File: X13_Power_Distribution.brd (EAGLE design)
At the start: 152.4 x 73.7 mm, 44 parts, among them Q1 IRF1018EPBF, Q2 SSM3K341R, Q3 IRF1018EPBF, Q4 IRF1018EPBF, Q5 SSM3K341R, Q6 SSM3K341R, U1 LM74610, U2 LM74610, U3 LM5050, U4 LM5050

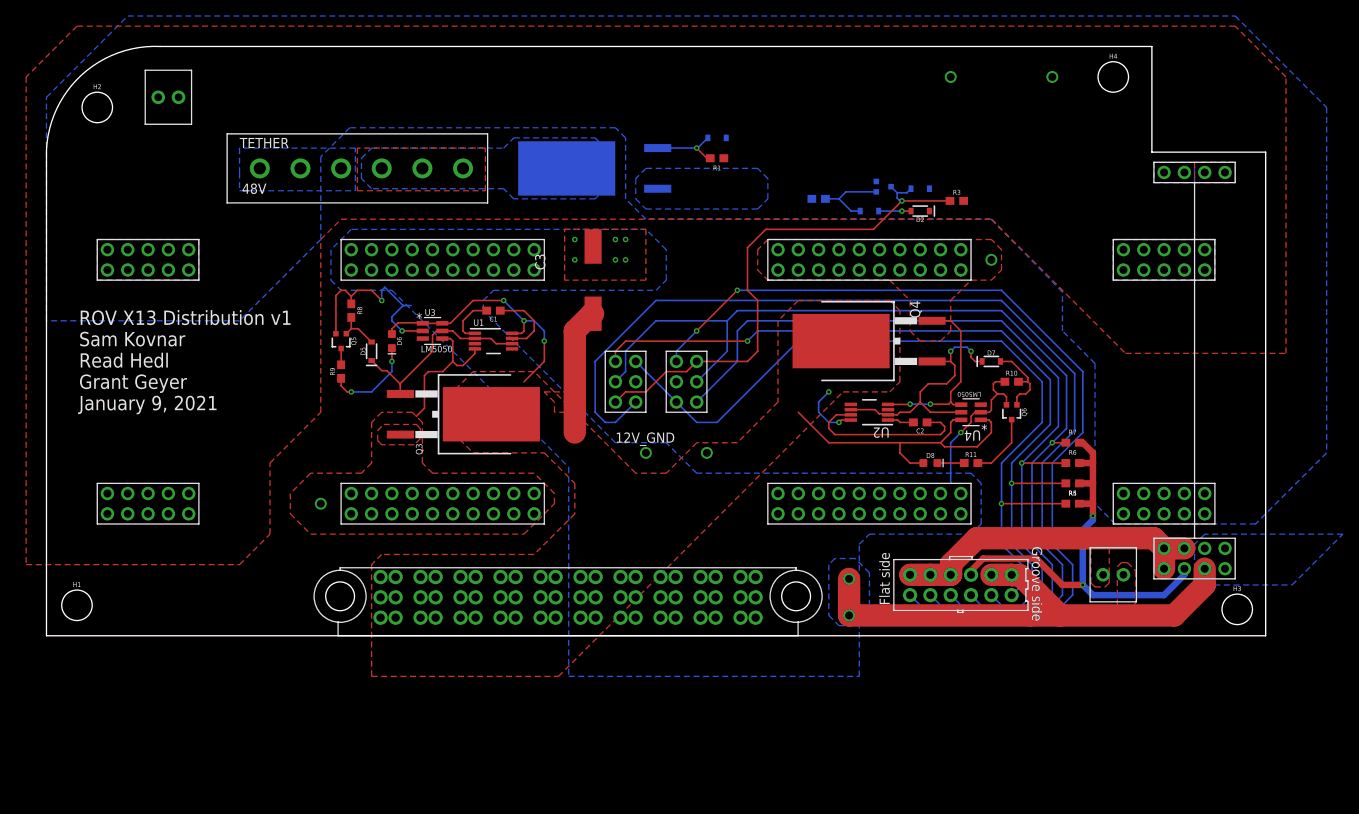
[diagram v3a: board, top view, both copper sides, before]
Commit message: Made some slight changes to thermals
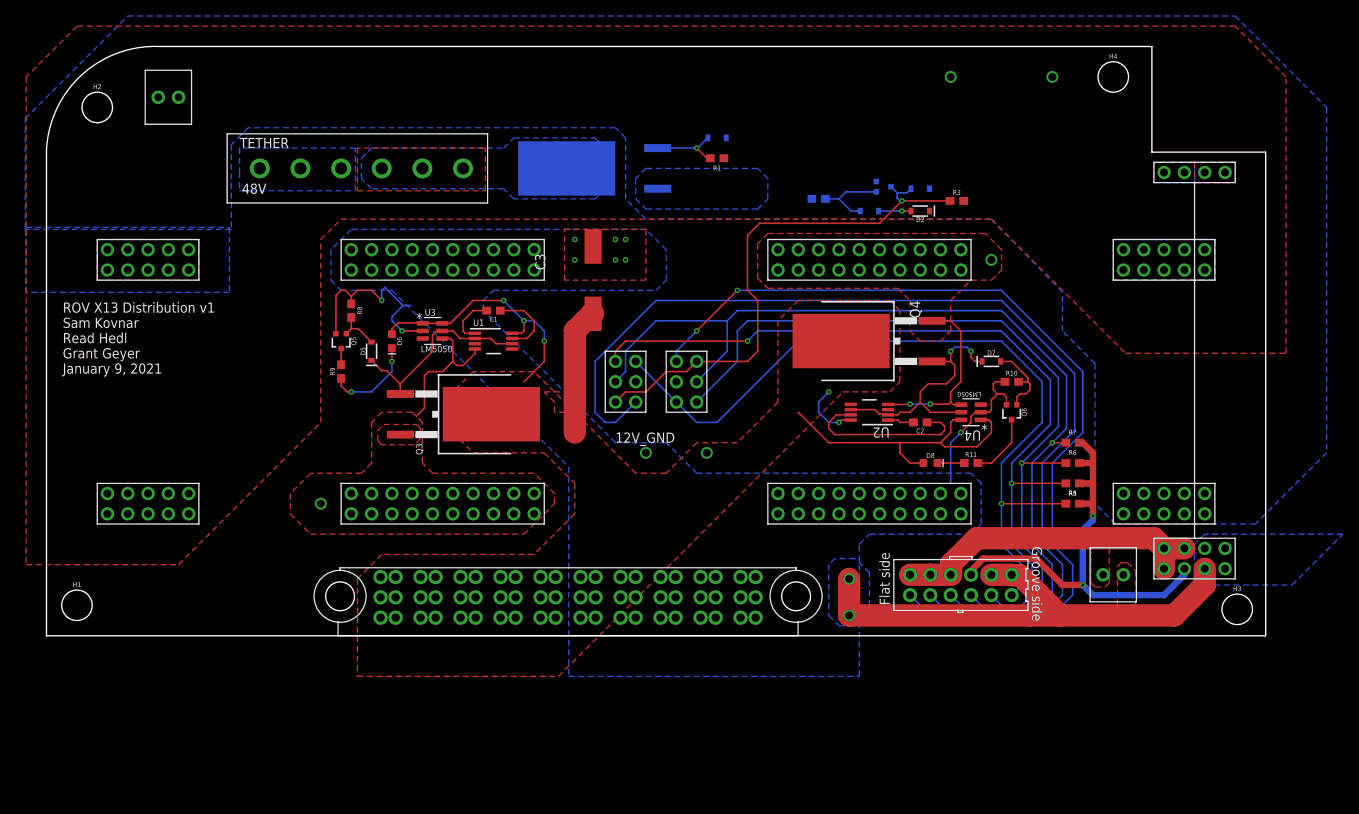
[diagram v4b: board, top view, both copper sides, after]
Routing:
- net ON/OFF: track 66.1 -> 67.0 mm

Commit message: Some more edits
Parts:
- added +12V_A_TEST, +12V_B_TEST, +12V_TEST, +48V_TEST, 12_GND, 48GND_TEST: SSW-101-02-G-S, con-samtec:SSW-101-02-G-S
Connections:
- net +12V: now also +12V_TEST.1
- net +12V_A: now also +12V_A_TEST.1
- net +12V_B: now also +12V_B_TEST.1
- net +48V: now also +48V_TEST.1
- net 12V_GND: now also 12_GND.1
- net 48V_GND: now also 48GND_TEST.1
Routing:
- net +48V: track 0.00 -> 15.6 mm
- net 12V_GND: vias 10 -> 9
- net +12V_B: vias 3 -> 2
- net +12V_A: vias 1 -> 0
- net +12V: vias 6 -> 5

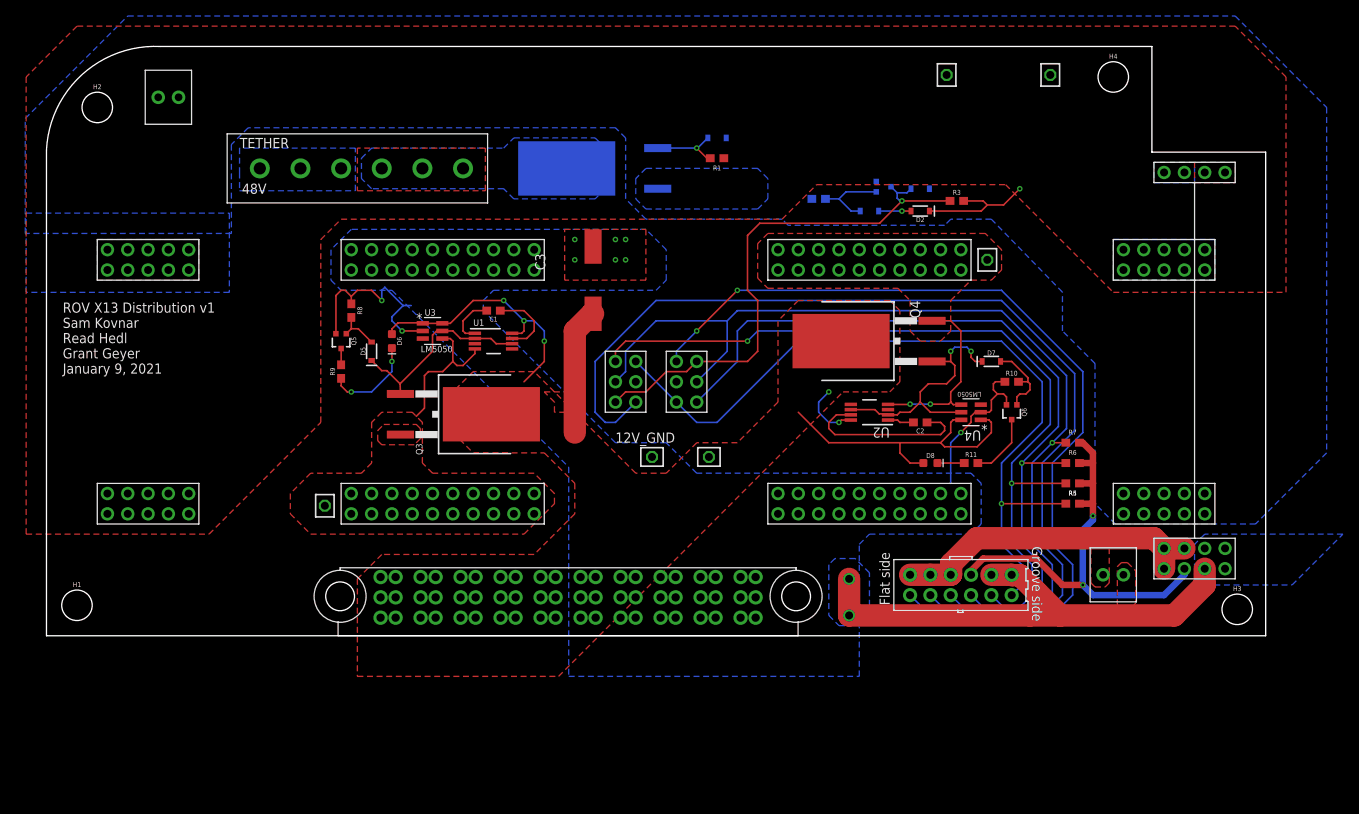
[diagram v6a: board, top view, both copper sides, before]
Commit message: Lower on/off threshold, remove old unused or-ing controller, try new 12V on LED circuit
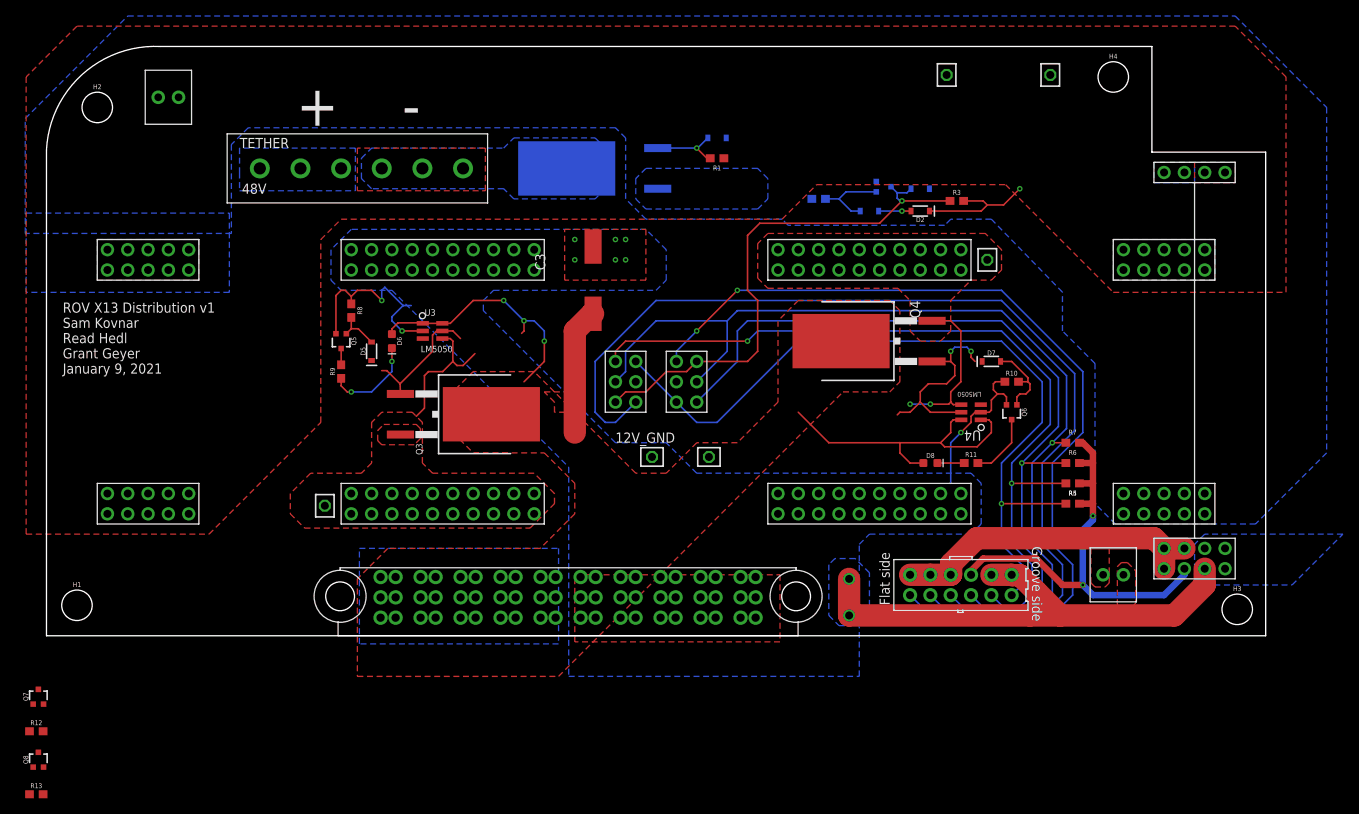
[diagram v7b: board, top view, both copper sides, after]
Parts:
- removed C1, C2: 2.2uF, SparkFun-Capacitors:0603
- removed U1, U2: LM74610, Dist_OR_Controller:DGK0008A_M
- added Q7, Q8: SSM3K341R, SparkFun-DiscreteSemi:SOT323
- added R12, R13: 10k, SparkFun-Resistors:0603
- D2, D3: value 22V -> 19V
- R10, R8: value 1M -> 10k
- U3, U4: device Dist_OR_Controller:MK06A-M -> Dist_OR_Controller:SOT-23-6
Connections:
- removed net VCAPH_A: C1.1, U1.7
- removed net VCAPH_B: C2.1, U2.7
- removed net VCAPL_A: C1.2, U1.1
- removed net VCAPL_B: C2.2, U2.1
- new net N$2: D5.C, Q7.2, R12.2
- new net N$3: D7.C, Q8.2, R13.2
- net +12V: no longer U1.8, U2.8
- net +12V_A: no longer U1.4
- net +12V_B: no longer U2.4
- net +48V: now also Q7.3, Q8.3
- net 12V_GND: now also R12.1, R13.1
- net OR_DRIVE_A: now also Q7.1; no longer D5.C, U1.2, U1.6
- net OR_DRIVE_B: now also Q8.1; no longer D7.C, U2.2, U2.6
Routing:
- net VCAPH_B: track 21.8 -> 0.00 mm
- net VCAPH_A: track 9.17 -> 0.00 mm
- net +12V: track 95.3 -> 86.4 mm, vias 5 -> 3
- net OR_DRIVE_A: track 24.6 -> 16.1 mm
- net OR_DRIVE_B: track 32.6 -> 25.6 mm
- net VCAPL_A: track 6.36 -> 0.00 mm
- net VCAPL_B: track 3.30 -> 0.00 mm
- net +12V_B: track 23.0 -> 20.2 mm
- net +12V_A: track 18.0 -> 17.4 mm
- added copper zone on layer 16, net +12V
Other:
- board text added: "+ -"

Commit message: Add solder jumper to short on/off and diode to latch voltage
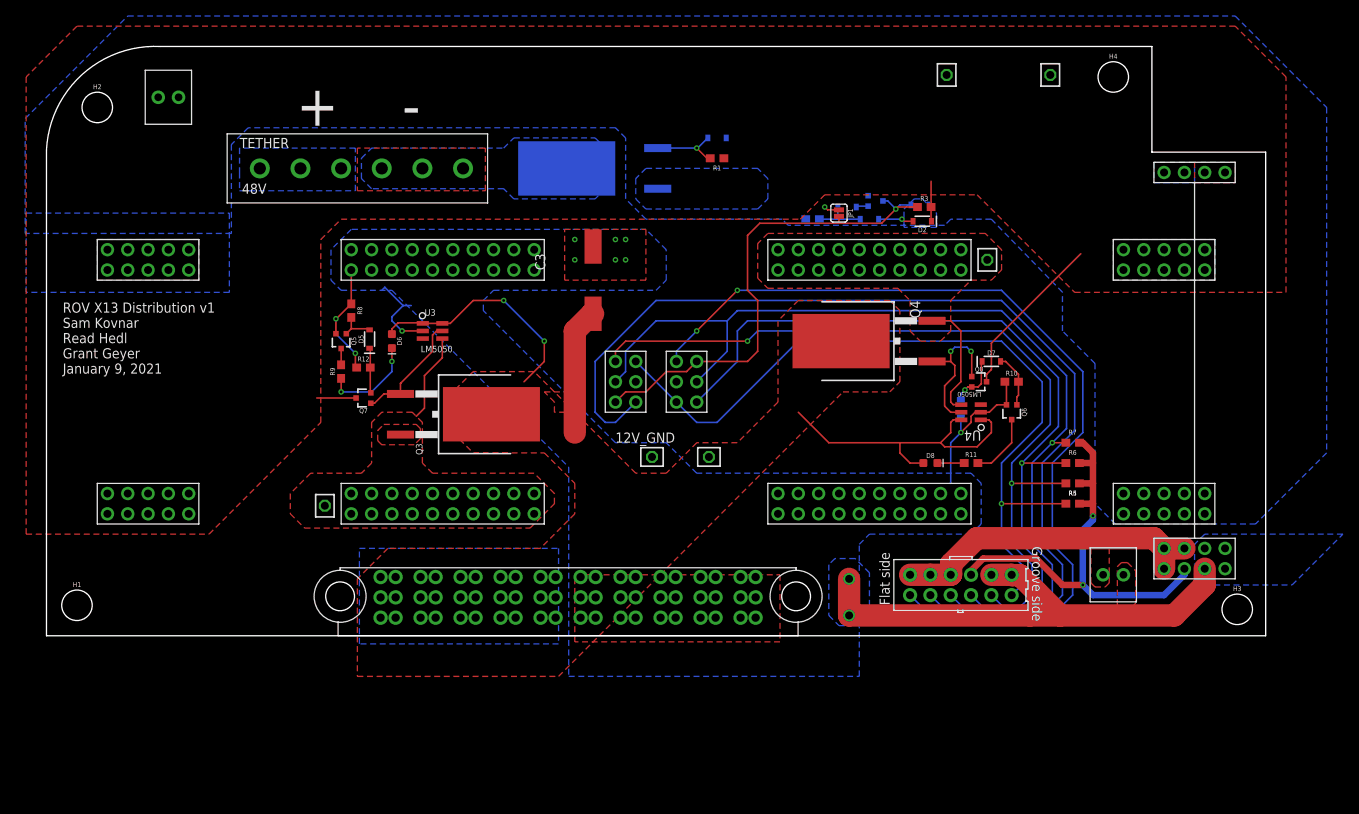
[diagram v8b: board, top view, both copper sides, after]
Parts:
- added D9: 250mA/100V, SparkFun-DiscreteSemi:SOD-323
- added JP1: JUMPER-SMT_2_NO_SILK, SparkFun-Jumpers:SMT-JUMPER_2_NO_SILK
- moved Q8 126.7 mm to (116.6, 31.8), turned to 270 degrees
- moved R13 125.2 mm to (114.3, 28.4), flipped to the bottom, turned to 90 degrees
- moved R12 61.2 mm to (39.6, 33.5)
- moved Q7 55.2 mm to (39.6, 29.7), turned to 90 degrees
- moved R3 4.13 mm to (109.7, 53.6)
- moved R2 2.65 mm to (95.8, 52.1)
- moved Q2 2.05 mm to (103.6, 54.4)
- moved D4 2.03 mm to (109.2, 53.8)
- moved D5 1.55 mm to (40.4, 37.1)
- moved D2 1.30 mm to (109.5, 51.8)
- moved D3 1.02 mm to (102.9, 52.1)
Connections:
- new net ON_DETECT: D3.A, D9.A, R2.2
- net 48V_GND: now also JP1.1
- net ON/OFF: now also JP1.2
- net ON/OFF_DRIVE: now also D9.C; no longer D3.A, R2.2
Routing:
- net +48V: track 15.6 -> 30.8 mm, vias 1 -> 0
- net ON/OFF_DRIVE: track 10.0 -> 1.53 mm
- net OR_DRIVE_B: track 25.6 -> 18.5 mm
- net N$3: track 0.00 -> 6.88 mm, vias 0 -> 1
- net ON_DETECT: track 0.00 -> 6.69 mm
- net +12V_A: track 17.4 -> 11.1 mm
- net N$2: track 0.00 -> 5.63 mm
- net +12V_B: track 20.2 -> 15.0 mm, vias 2 -> 0
- net ON/OFF: track 67.0 -> 63.4 mm
- net LED_DRIVE_B: track 10.1 -> 6.80 mm
- net +12V: track 86.4 -> 84.0 mm, vias 3 -> 2
- net 48V_GND: track 0.00 -> 1.93 mm, vias 0 -> 1
- net 12V_GND: track 45.7 -> 47.2 mm, vias 9 -> 10
- net OR_DRIVE_A: track 16.1 -> 14.6 mm
- net LED_DRIVE_A: track 5.52 -> 4.64 mm
- added copper zone on layer 16, net X
